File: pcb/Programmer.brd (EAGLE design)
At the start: 160 x 100 mm, 47 parts, among them J1 MINI-USB-JACK, U1 FT232HQ, U10 TPD4S012DRYR, U2 SN74LV1T125DCKR, U3 SN74LV1T125DCKR, U4 SN74LV1T125DCKR, U5 SN74LV1T125DCKR, U6 SN74LV1T125DCKR, U7 SN74LV1T125DCKR, U8 SN74LV1T126DCKR, U9 SN74LV1T126DCKR, X1 SIT8021

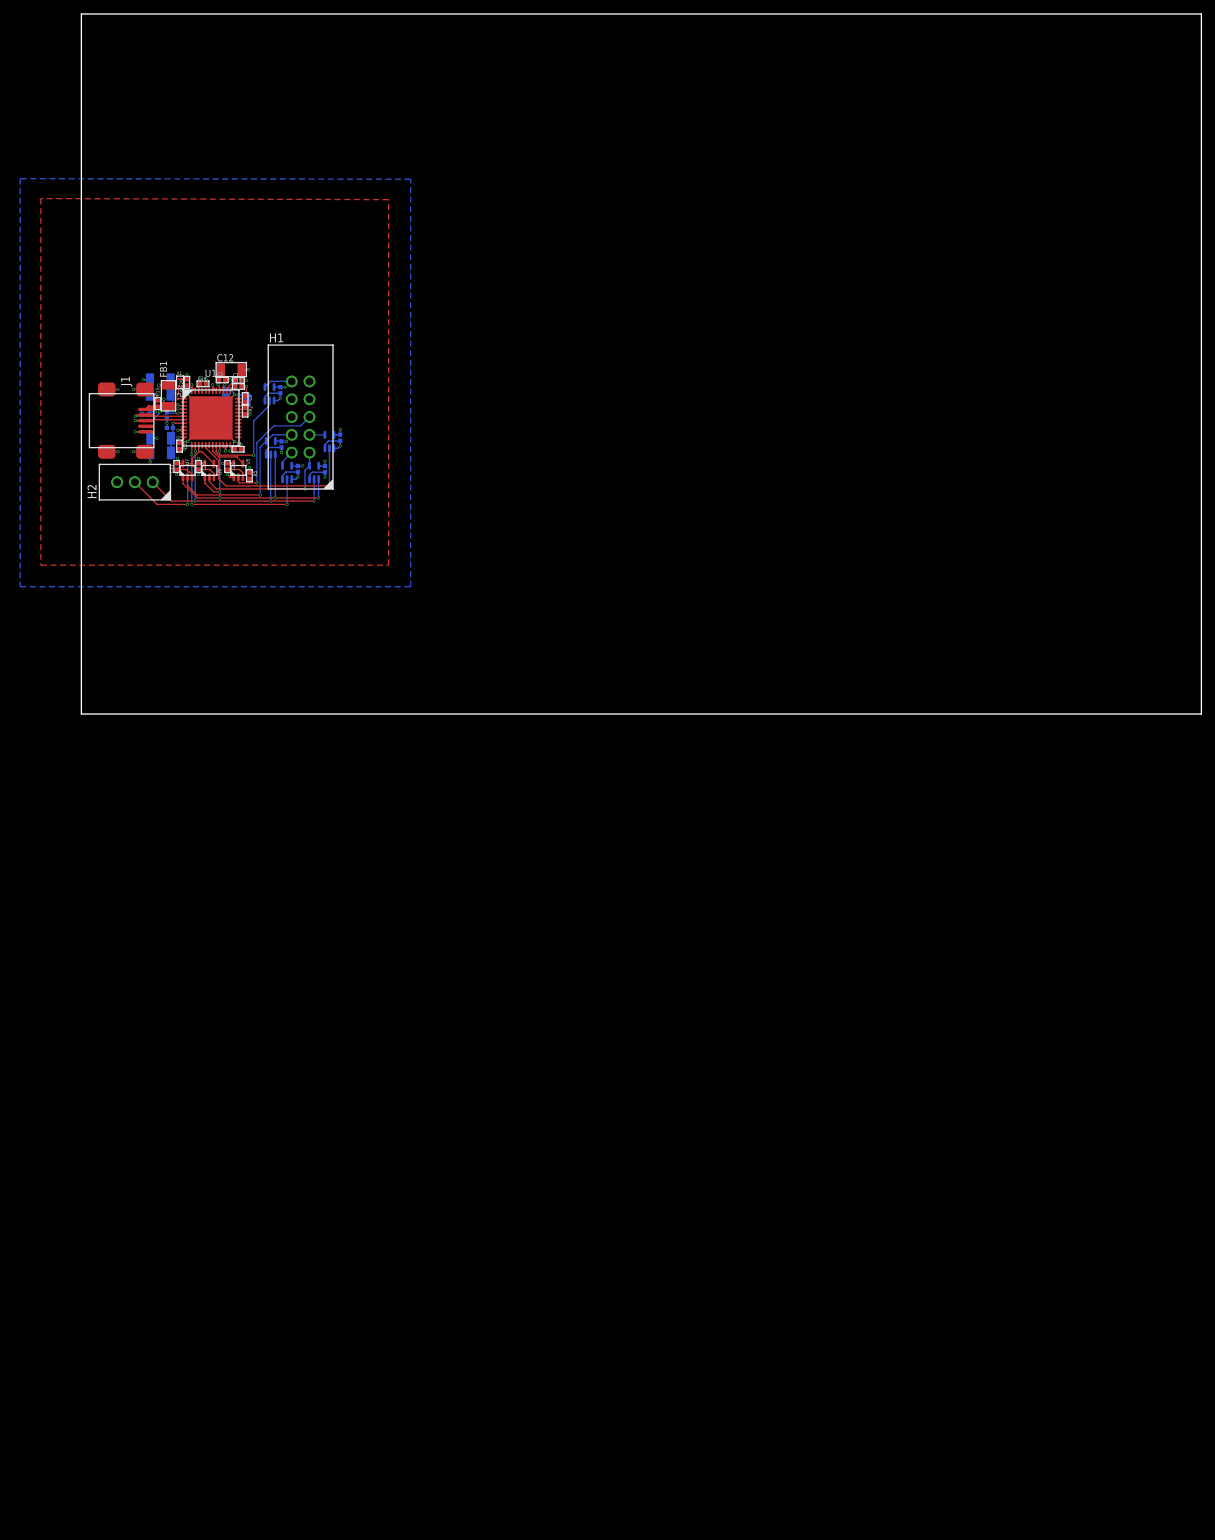
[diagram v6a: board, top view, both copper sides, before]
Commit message: Programmer: Place silkscreen labels
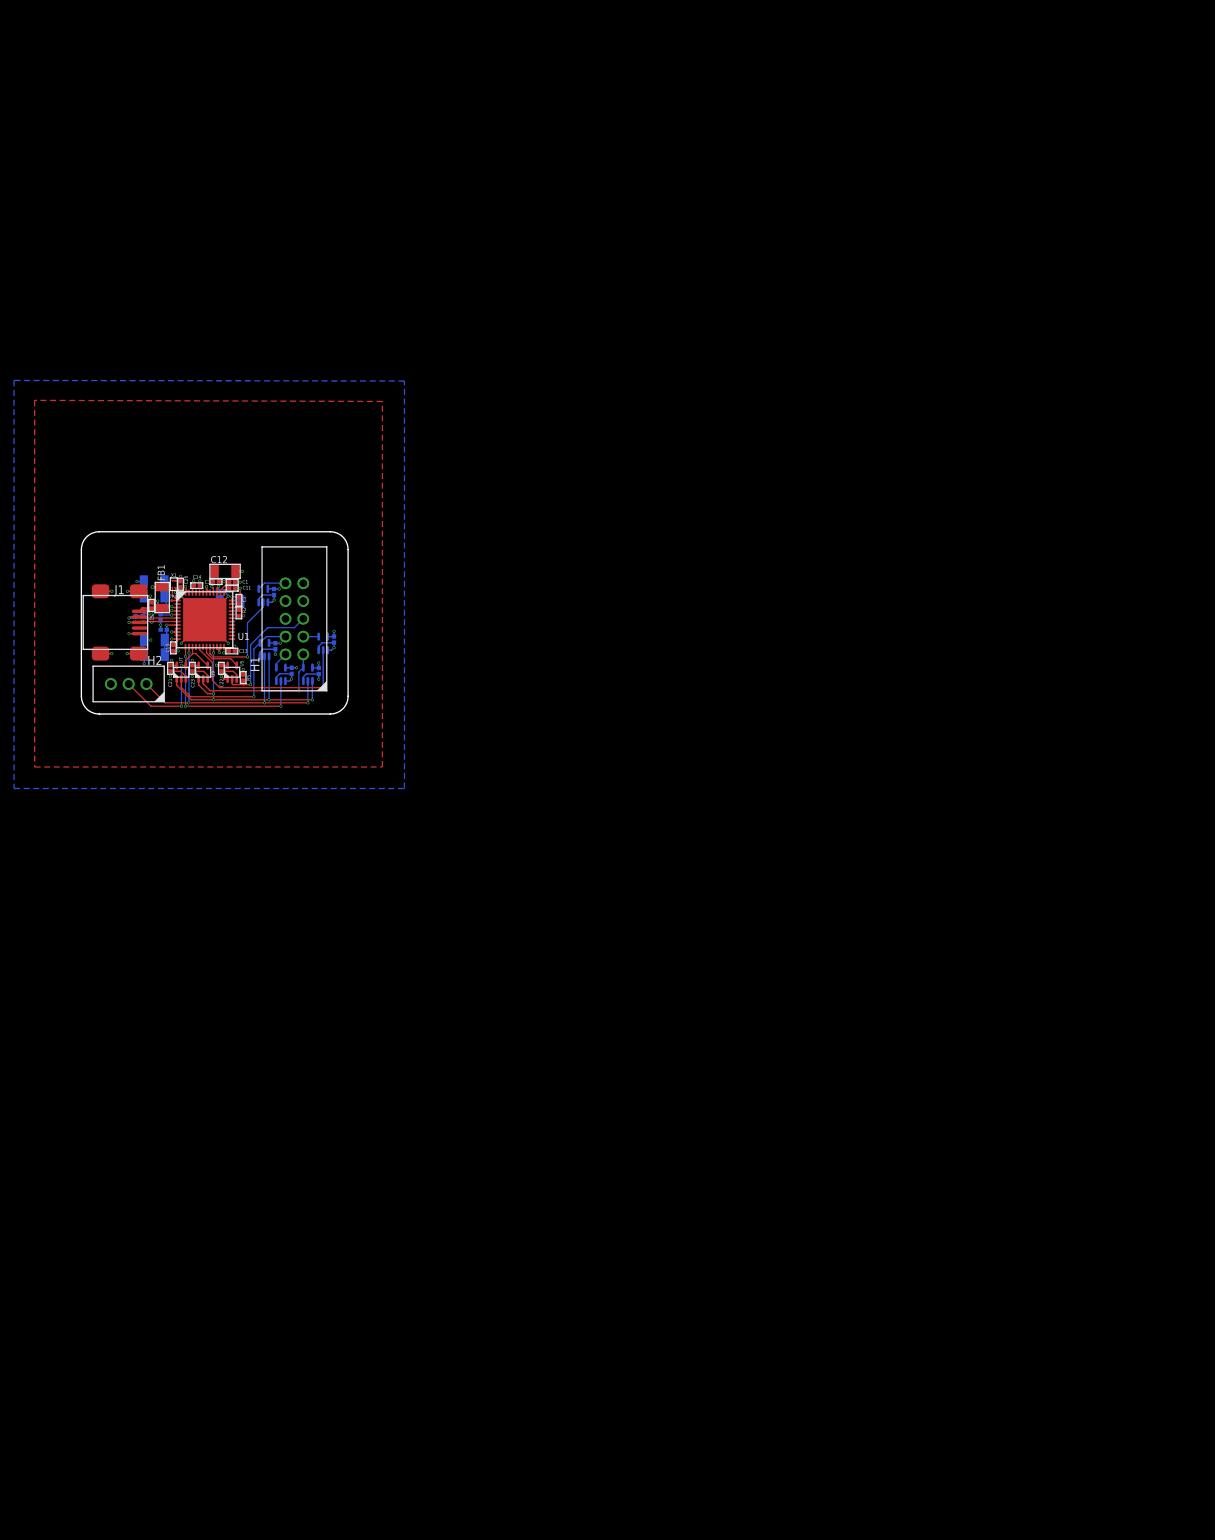
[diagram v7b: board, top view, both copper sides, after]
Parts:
- moved C12 28.8 mm to (20.5, 20.4)
- moved C2 28.8 mm to (22.5, 16.2)
- moved C8 28.8 mm to (21.2, 16.1)
- moved FB2 28.8 mm to (10.4, 18.9)
- moved FB3 28.8 mm to (10.4, 8.48)
- moved C10 28.8 mm to (13.1, 9.45)
- moved C11 28.8 mm to (21.5, 18.0)
- moved C13 28.8 mm to (21.5, 8.99)
- moved C14 28.8 mm to (16.5, 18.3)
- moved C15 28.8 mm to (10.0, 15.5)
- moved C17 28.8 mm to (33.9, 6.15)
- moved C18 28.8 mm to (36.1, 10.6)
- moved C19 28.8 mm to (27.5, 17.4)
- moved C20 28.8 mm to (27.7, 9.68)
- moved C21 28.8 mm to (12.7, 6.53)
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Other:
- board size 160 x 100 mm -> 38.1 x 26 mm
